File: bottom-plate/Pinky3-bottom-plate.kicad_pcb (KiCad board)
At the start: 2 copper layers, 137 x 100.9 mm, 5 parts

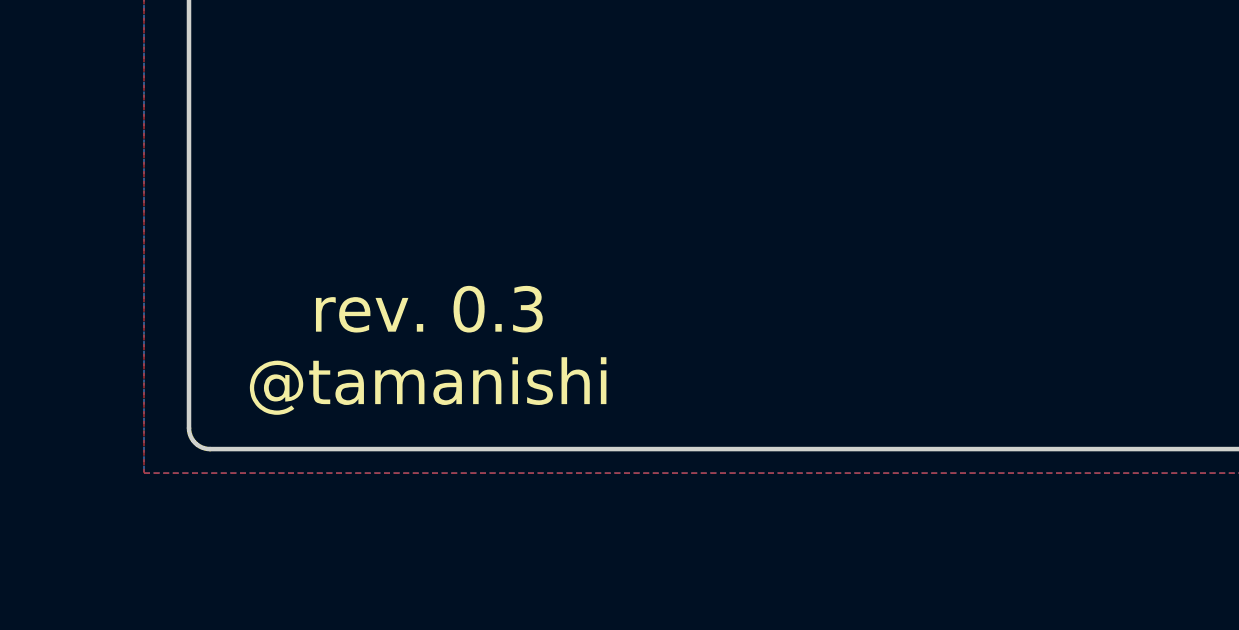
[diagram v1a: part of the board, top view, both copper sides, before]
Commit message: - add images - add logo - change thumb keys footprints to choc only
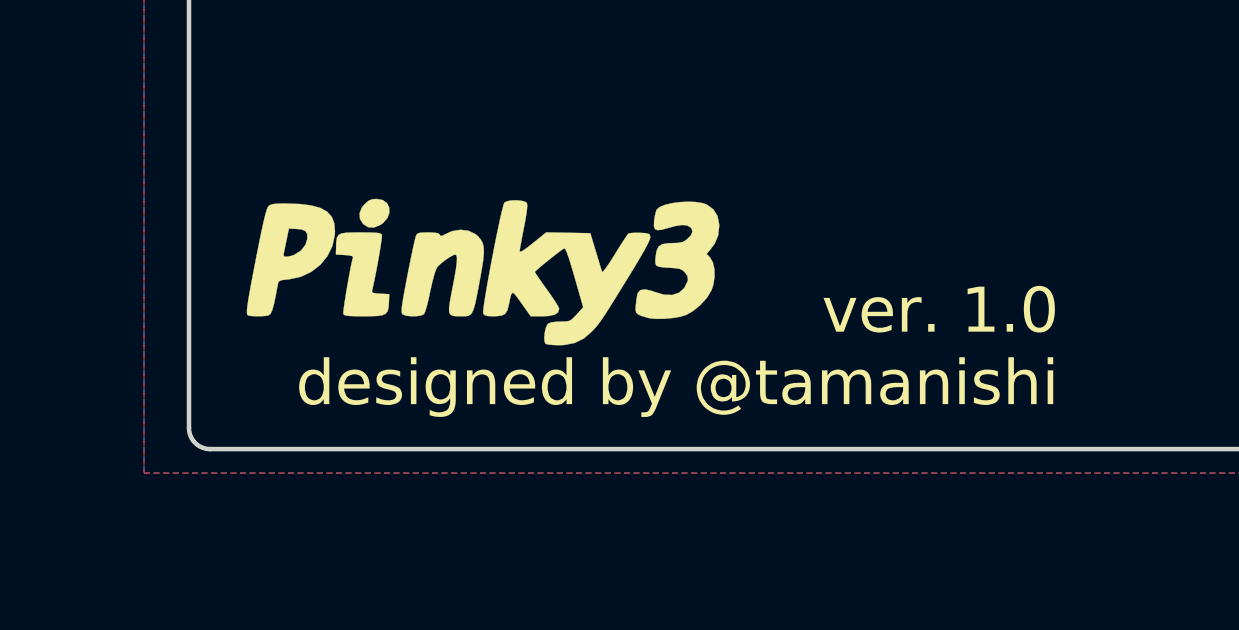
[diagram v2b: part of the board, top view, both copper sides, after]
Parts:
- added G***: LOGO, lib:pinky3, B.Cu at (61.5, 130.4)
- added G***: LOGO, lib:pinky3, F.Cu at (50.8, 130.4)
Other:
- board text added: "ver. 1.0 designed by @tamanishi"
- board text removed: "rev. 0.3 @tamanishi"
